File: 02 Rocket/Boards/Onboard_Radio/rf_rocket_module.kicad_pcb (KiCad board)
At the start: 4 copper layers, 65 x 50 mm, 91 parts, among them J10 M80, J11 MICROFIT, J3 USB_B_Micro, J4 SWD JST PH, J5 MICROFIT, J6 RFIO SMA, J9 M80, U1 TCAN1046, U2 SX1262, U3 PE4259 RF Switch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

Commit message: idk aye
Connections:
- J11 pad 1: /Power Input/+7V4_In -> /Power Input/+V_In
- R20 pad 1: /Power Input/+7V4_In -> /Power Input/+V_In
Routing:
- net /Power Input/+V_In: track 8.15 -> 25.0 mm
- net /Power Input/+7V4_In: track 5.71 -> 0.00 mm
- net GND: track 71.8 -> 76.2 mm, vias 121 -> 124
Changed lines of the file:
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@@
 		(capping no)
 		(filling no)
-		(zone_defaults)
 		(pcbplotparams
 			(layerselection 0x00000000_00000000_55555555_5755f5ff)
@@
 			(remove_unused_layers no)
 			(roundrect_rratio 0.166667)
-			(net "/Power Input/+7V4_In")
+			(net "/Power Input/+V_In")
 			(pinfunction "Pin_1_1")
 			(pintype "power_out")
@@
 			(layers "F.Cu" "F.Mask" "F.Paste")
 			(roundrect_rratio 0.25)
-			(net "/Power Input/+7V4_In")
+			(net "/Power Input/+V_In")
 			(pintype "passive")
 		)
@@
 	)
 	(segment
+		(start 168.4 130.785)
+		(end 168.4 130.8)
+		(width 0.1422)
+		(layer "F.Cu")
+		(net "GND")
+	)
+	(segment
 		(start 152.725 115.325)
 		(end 151.625 115.325)
@@
 	)
 	(segment
+		(start 167.4 129.785)
+		(end 168.4 130.785)
+		(width 0.1422)
+		(layer "F.Cu")
+		(net "GND")
+	)
+	(segment
 		(start 175.7 122.605)
 		(end 174.83 122.605)
@@
 	)
 	(segment
+		(start 176.1 132.755)
+		(end 175.055 133.8)
+		(width 0.1422)
+		(layer "F.Cu")
+		(net "GND")
+	)
+	(segment
 		(start 155.325 106.092038)
 		(end 155.294451 106.061489)
@@
 	)
 	(segment
+		(start 175.055 133.8)
+		(end 175 133.8)
+		(width 0.1422)
+		(layer "F.Cu")
+		(net "GND")
+	)
+	(segment
 		(start 168.525 117.925)
 		(end 168.175 117.925)
@@
 	)
 	(segment
+		(start 180.1 130.755)
+		(end 180.1 130.8)
+		(width 0.1422)
+		(layer "F.Cu")
+		(net "GND")
+	)
+	(segment
 		(start 185.5 112)
 		(end 187.115 112)
@@
 	)
 	(segment
+		(start 179.1 129.755)
+		(end 180.1 130.755)
+		(width 0.1422)
+		(layer "F.Cu")
+		(net "GND")
+	)
+	(segment
 		(start 154.65 117.05)
 		(end 154.2 117.05)
@@
 	)
 	(via
+		(at 175 133.8)
+		(size 0.6)
+		(drill 0.3)
+		(layers "F.Cu" "B.Cu")
+		(net "GND")
+	)
+	(via
 		(at 160.6 95)
 		(size 0.6)
@@
 	)
 	(via
+		(at 180.1 130.8)
+		(size 0.6)
+		(drill 0.3)
+		(layers "F.Cu" "B.Cu")
+		(net "GND")
+	)
+	(via
 		(at 152.5 93.25)
 		(size 0.6)
@@
 	)
 	(via
+		(at 168.4 130.8)
+		(size 0.6)
+		(drill 0.3)
+		(layers "F.Cu" "B.Cu")
+		(net "GND")
+	)
+	(via
 		(at 171.725 110.775)
 		(size 0.6)
@@
 	)
 	(segment
+		(start 167.2 126.7)
+		(end 167.2 125.705)
+		(width 0.2)
+		(layer "F.Cu")
+		(net "/Power Input/+V_In")
+	)
+	(segment
 		(start 176.1 129.755)
 		(end 176.306336 129.755)
@@
 	)
 	(segment
+		(start 170.255 129.755)
+		(end 167.2 126.7)
+		(width 0.2)
+		(layer "F.Cu")
+		(net "/Power Input/+V_In")
+	)
+	(segment
+		(start 164.4 129.785)
+		(end 164.4 127.7)
+		(width 0.2)
+		(layer "F.Cu")
+		(net "/Power Input/+V_In")
+	)
+	(segment
+		(start 176.1 129.755)
+		(end 170.255 129.755)
+		(width 0.2)
+		(layer "F.Cu")
+		(net "/Power Input/+V_In")
+	)
+	(segment
+		(start 164.4 127.7)
+		(end 166.395 125.705)
+		(width 0.2)
+		(layer "F.Cu")
+		(net "/Power Input/+V_In")
+	)
+	(segment
+		(start 166.395 125.705)
+		(end 167.2 125.705)
+		(width 0.2)
+		(layer "F.Cu")
+		(net "/Power Input/+V_In")
+	)
+	(segment
 		(start 176.306336 129.755)
 		(end 180.55 125.511336)
@@
 	)
 	(segment
-		(start 164.4 129.785)
-		(end 164.4 127.7)
-		(width 0.2)
-		(layer "F.Cu")
-		(net "/Power Input/+7V4_In")
-	)
-	(segment
-		(start 164.4 127.7)
-		(end 166.395 125.705)
-		(width 0.2)
-		(layer "F.Cu")
-		(net "/Power Input/+7V4_In")
-	)
-	(segment
-		(start 166.395 125.705)
-		(end 167.2 125.705)
-		(width 0.2)
-		(layer "F.Cu")
-		(net "/Power Input/+7V4_In")
-	)
-	(segment

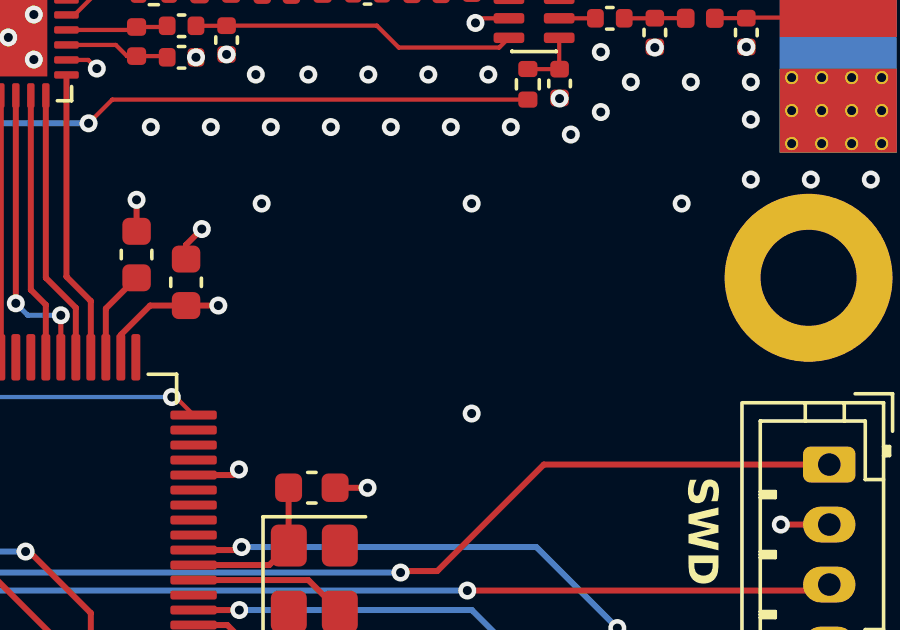
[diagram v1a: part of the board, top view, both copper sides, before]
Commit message: rocket, gs, jpole need review b4 order, update last of bom
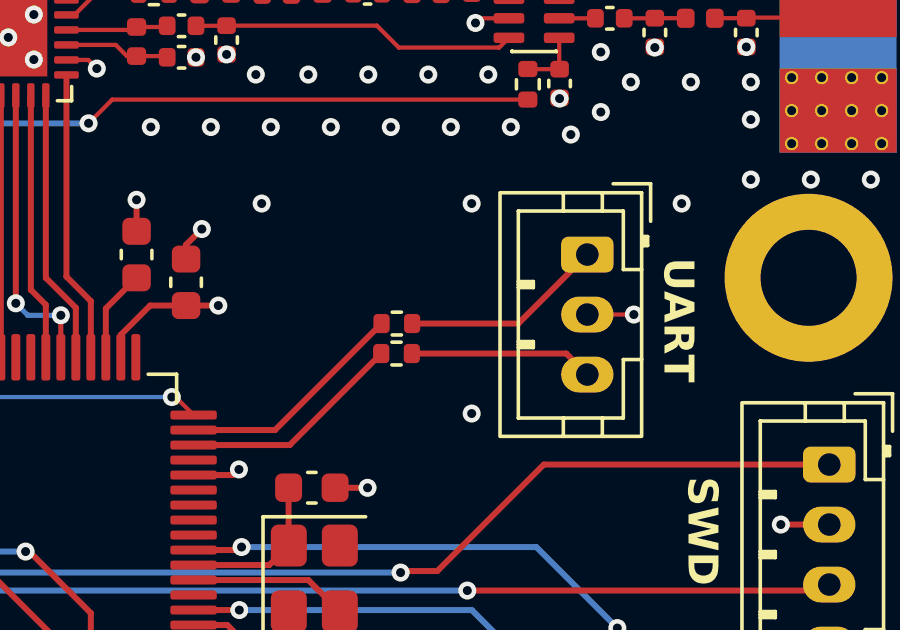
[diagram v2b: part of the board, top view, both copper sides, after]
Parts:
- added J15: UART JST, Connector_JST:JST_PH_B3B-PH-K_1x03_P2.00mm_Vertical, F.Cu at (179.1, 103.0)
- added R2: 0R, Resistor_SMD:R_0402_1005Metric, F.Cu at (172.7, 106.3)
- added R5: 0R, Resistor_SMD:R_0402_1005Metric, F.Cu at (172.7, 105.3)
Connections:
- U4 pad 14: unconnected-(U4-PA0-Pad14) -> Net-(U4-PA0)
- U4 pad 15: unconnected-(U4-PA1-Pad15) -> Net-(U4-PA1)
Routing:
- net Net-(U4-PA1): track 0.00 -> 7.74 mm
- net Net-(U4-PA0): track 0.00 -> 7.52 mm
- net /MCU/UART_RX: track 0.00 -> 6.79 mm
- net /MCU/UART_TX: track 0.00 -> 6.14 mm
- net GND: track 76.2 -> 77.7 mm, vias 124 -> 125
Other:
- board text added: "UART"

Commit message: Narottam Updates Resolved
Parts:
- removed R10, R11: 27R, Resistor_SMD:R_0603_1608Metric
- removed R20: 0R, Resistor_SMD:R_0603_1608Metric
- added D5: LED_Y, LED_SMD:LED_0603_1608Metric, F.Cu at (132.0, 123.4)
- added R17: 549R, Resistor_SMD:R_0603_1608Metric, F.Cu at (132.0, 120.3)
- U5, U6: value MIC5365-3.3YC5 -> SC573V33RTRC
- U7: value AS78L05RTR-E1 -> MC78M05BDTRKG; footprint Package_TO_SOT_SMD:SOT-89-3 -> Package_TO_SOT_SMD:TO-252-3_TabPin2
- Y1: footprint Crystal:Crystal_SMD_Abracon_ABM8G-4Pin_3.2x2.5mm -> Oscillator:Oscillator_SMD_ECS_2520MV-xxx-xx-4Pin_2.5x2.0mm
- moved JP3 23.2 mm to (168.0, 100.8)
- moved C19 20.8 mm to (126.2, 99.4), turned to 180 degrees
- moved U5 20.8 mm to (163.2, 104.8), turned to 180 degrees
- moved U7 18.2 mm to (168.5, 108.7)
- moved R7 17.3 mm to (124.9, 95.0), turned to -90 degrees
- moved C23 17.0 mm to (153.9, 91.7), turned to 90 degrees
- moved C35 16.5 mm to (163.7, 110.4)
- moved C39 16.3 mm to (162.4, 113.6)
- moved C36 16.3 mm to (164.0, 113.6)
- moved C24 16.3 mm to (152.3, 91.7), turned to 90 degrees
- moved C18 16.2 mm to (144.9, 84.7), turned to 180 degrees
- moved C27 16.1 mm to (141.5, 104.5)
- moved J15 16.1 mm to (167.8, 91.4)
- moved R2 16.1 mm to (161.5, 94.7)
- moved C28 16.1 mm to (143.0, 106.2), turned to -90 degrees
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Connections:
- net /+3V3A renamed +3V3A
- C20 pad 1: +3V3 -> GND
- C23 pad 1: +3V3 -> GND
- C24 pad 1: +3V3 -> GND
- C25 pad 1: +3V3 -> GND
- C26 pad 1: +3V3 -> GND
- C27 pad 1: +3V3 -> GND
- C28 pad 1: +3V3 -> GND
- C29 pad 1: +3V3 -> GND
- C30 pad 1: +3V3 -> GND
- F2 pad 1: +7V4 -> +5V
- JP3 pad 2: +3V3 -> GND
- R14 pad 1: +7V4 -> +5V
- R9 pad 2: +3V3 -> GND
- U1 pad 3: +3V3 -> GND
- U4 pad 44: /MCU/MCU_D- -> /MCU/USB_D-
- U4 pad 45: /MCU/MCU_D+ -> /MCU/USB_D+
- U4 pad 46: /MCU/SWCLK -> /MCU/SWDIO
- U4 pad 49: /MCU/SWDIO -> /MCU/SWCLK
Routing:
- net +7V4: track 38.4 -> 0.00 mm, vias 2 -> 0
- net GND: track 77.7 -> 111.4 mm, vias 125 -> 145
- net +3V3: track 17.2 -> 0.00 mm, vias 11 -> 0
- net /MCU/MCU_D-: track 14.9 -> 0.00 mm
- net /MCU/MCU_D+: track 14.9 -> 0.00 mm
- net /MCU/USB_D-: track 9.92 -> 23.0 mm
- net /MCU/USB_D+: track 9.96 -> 22.4 mm
- net +5V: track 51.7 -> 63.0 mm
- net +3V3A: track 43.8 -> 36.7 mm
- net /MCU/3V3_LDO_EN: track 16.3 -> 9.87 mm
- net /Power Input/+3V3_In: track 21.4 -> 27.3 mm
- net /LoRav2/XTB: track 7.09 -> 2.73 mm
- net Net-(JP7-B): track 5.71 -> 2.49 mm
- net /CAN_Termination/CANL: track 7.91 -> 10.6 mm
- net Net-(JP5-A): track 4.57 -> 2.27 mm
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- added copper zone on In2.Cu, net +3V3A
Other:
- board text added: "+3V3"
- board text added: "+5V"
- board text removed: "+7V4"

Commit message: radio board ordered!
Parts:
- added R10: 10k, Resistor_SMD:R_0603_1608Metric, F.Cu at (161.4, 102.3)
- added R6: 10k, Resistor_SMD:R_0603_1608Metric, F.Cu at (157.5, 111.0)
- moved C29 1.82 mm to (154.1, 108.9)
- moved C30 1.79 mm to (152.5, 108.9), turned to 90 degrees
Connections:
- C20 pad 1: GND -> +3V3
- C23 pad 1: GND -> +3V3
- C24 pad 1: GND -> +3V3
- C25 pad 1: GND -> +3V3
- C26 pad 1: GND -> +3V3
- C27 pad 1: GND -> +3V3
- C28 pad 1: GND -> +3V3
- C29 pad 1: GND -> +3V3
- C30 pad 1: GND -> +3V3
- C40 pad 1: /Power Input/+V_In -> +7V4
- F2 pad 1: +5V -> +7V4
- J11 pad 1: /Power Input/+V_In -> +7V4
- J5 pad 1: /Power Input/+V_In -> +7V4
- JP3 pad 2: GND -> +3V3
- R17 pad 1: GND -> +3V3
- R9 pad 2: GND -> +3V3
- U1 pad 3: GND -> +3V3
- U4 pad 19: GND -> +3V3
- U4 pad 32: GND -> +3V3
- U4 pad 48: GND -> +3V3
- U4 pad 64: GND -> +3V3
- U7 pad 3: /Power Input/+V_In -> +7V4
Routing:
- net +7V4: track 0.00 -> 55.9 mm, vias 0 -> 1
- net +3V3: track 0.00 -> 28.0 mm, vias 0 -> 8
- net GND: track 111.4 -> 84.3 mm, vias 145 -> 136
- net /Power Input/+V_In: track 25.4 -> 0.00 mm
- net /Power Input/+5V_LDO: track 15.6 -> 24.9 mm
- net /MCU/3V3_LDO_EN: track 9.87 -> 17.5 mm, vias 2 -> 3
- net /MCU/3V3A_LDO_EN: track 12.8 -> 16.5 mm, vias 2 -> 3
- net +5V: track 63.0 -> 62.4 mm
